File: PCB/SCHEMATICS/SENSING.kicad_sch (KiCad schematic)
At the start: 7 parts, among them U3 LTR-303ALS-01

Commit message: Updated Schematics
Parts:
- removed R6: 1K, symbol Device:R_Small_US
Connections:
- net VBUS is gone; now on net +3.3V: R4.1, R5.1
- net 1 renamed Battery_sensor_output
- net PB10 renamed Light_sensor_SCL
- net PB11 renamed Light_sensor_SDA
- net PINSSSS renamed GND
- net V3OUT renamed +3.3V
- net Vout renamed Vbatt
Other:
- moved on the sheet: R7, R8

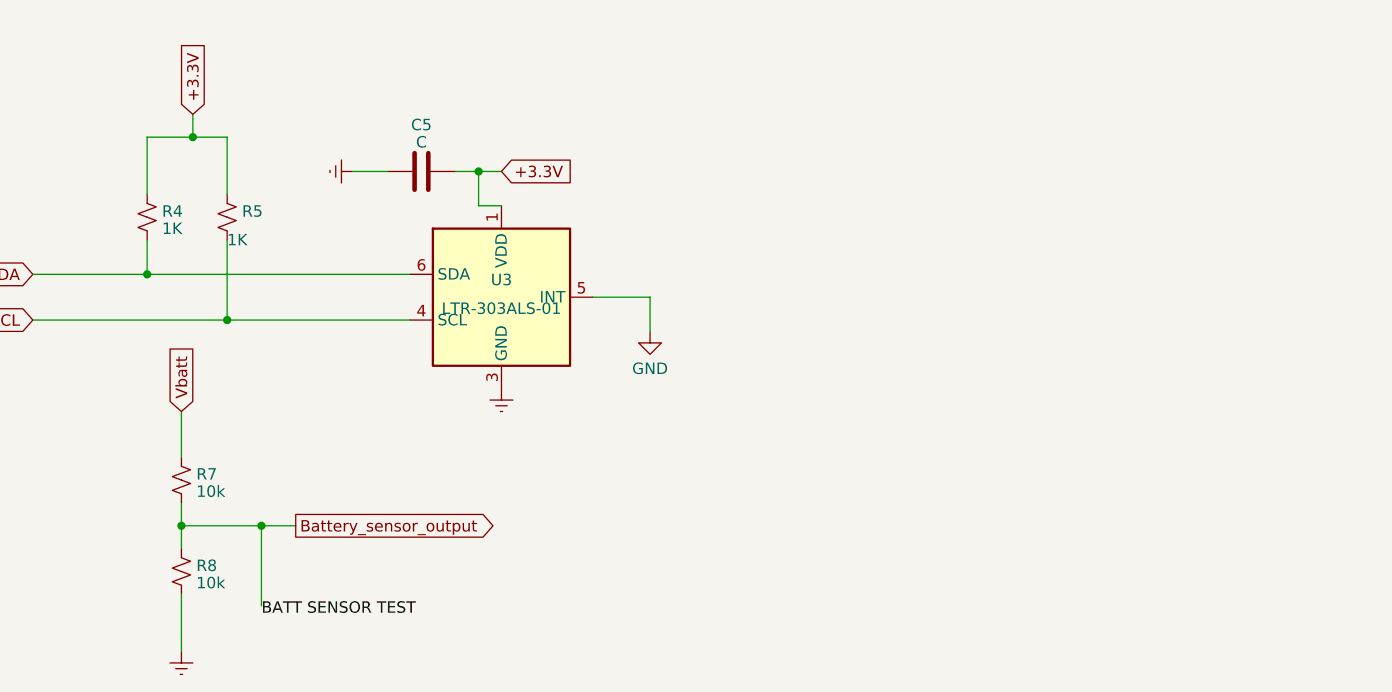
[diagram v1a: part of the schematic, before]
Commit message: UPDATED SCHEMATICS.
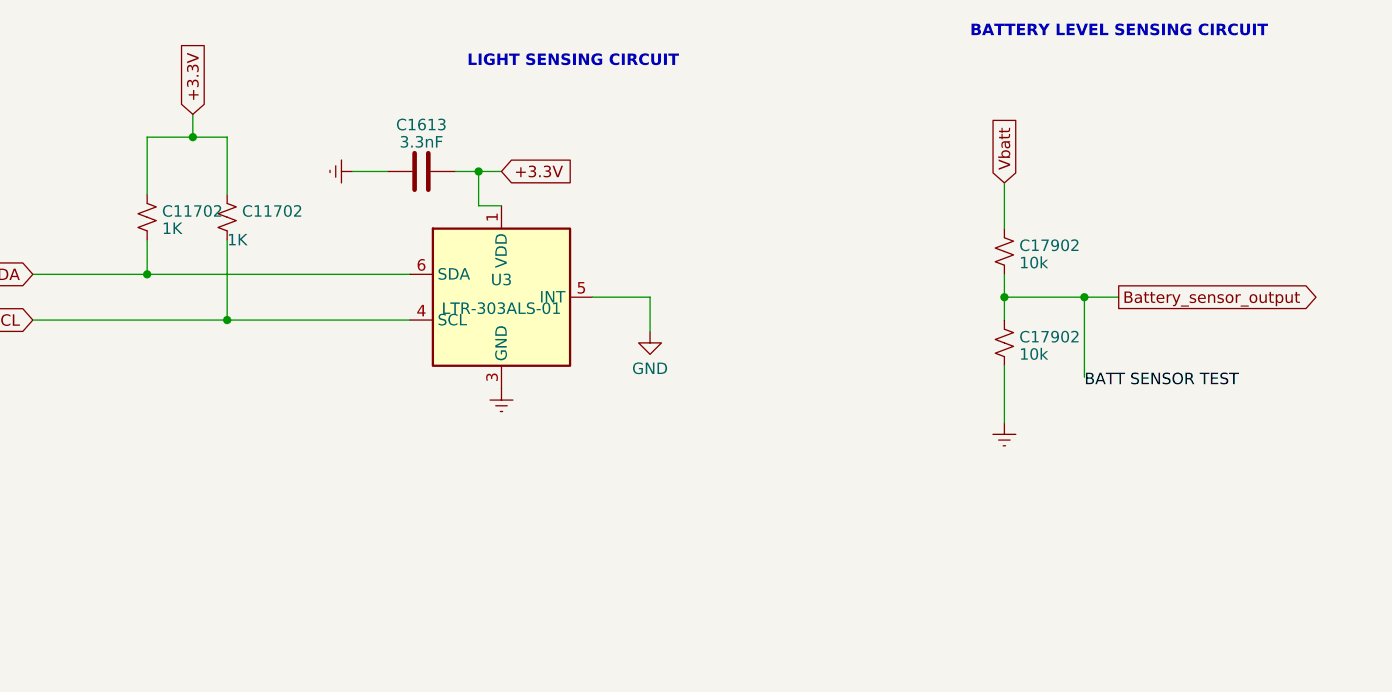
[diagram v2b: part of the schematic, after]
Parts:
- C11702: renamed from R4; Unit Price (none) -> 0.0005
- C11702: renamed from R5; Unit Price (none) -> 0.0005
- C1613: renamed from C5; value C -> 3.3nF; Unit Price (none) -> 0.0058
- C17902: renamed from R7; Unit Price (none) -> 0.003
- C17902: renamed from R8; Unit Price (none) -> 0.003
- U3: Extended (none) -> YES; Unit Price (none) -> 0.3887
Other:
- note added: "BATTERY LEVEL SENSING CIRCUIT"
- note added: "LIGHT SENSING CIRCUIT"
- moved on the sheet: C17902

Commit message: Updating schematics
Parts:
- added C1, C2: 1K, symbol Device:R_Small_US
- added C3: 3.3nF, symbol Device:C
- added TP1, TP2: TestPoint, symbol Connector:TestPoint
- added U5: LTR-303ALS-01, OptoDevice:Lite-On_LTR-303ALS-01, symbol Sensor_Optical:LTR-303ALS-01
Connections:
- net +3.3V: now also C1.1, C2.1, C3.2, U5.1 (VDD)
- net Earth: now also C3.1, U5.3 (GND)
- net GND: now also U5.5 (INT)
- new net: C1.2, TP1.1, U5.6 (SDA)
- new net: C2.2, TP2.1, U5.4 (SCL)

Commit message: Adjusted Schematics
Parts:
- added TP13, TP14, TP15, TP16, TP17, TP18, TP19, TP20, TP21: TestPoint, symbol Connector:TestPoint
- C17900: renamed from C17902; value 10k -> 100k
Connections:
- net Battery_sensor_output: now also TP21.1
- net Light_sensor_SCL: now also TP14.1, TP17.1
- net Light_sensor_SDA: now also TP15.1, TP16.1
- net +3.3V renamed 3V3
- net 3V3: now also TP13.1; no longer C1.1, C2.1, C3.2, U5.1 (VDD)
- net Vbatt renamed Battery
- net Battery: now also TP20.1
- new net: C3.2, TP18.1, U5.1 (VDD)
- new net: C1.1, C2.1, TP19.1
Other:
- note added: "Spare Light Sensor"
- moved on the sheet: C11702

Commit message: Updated schematics
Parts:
- C28323: renamed from C3; value 3.3nF -> 1uF
- C28323: renamed from C1613; value 3.3nF -> 1uF
- renumbered C1 to C11702, C2 to C11702
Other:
- company: (none) -> UCT
- title: (none) -> SENSING MODULE
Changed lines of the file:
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@@
 (kicad_sch (version 20230121) (generator eeschema)
   (paper "A4")
+  (title_block
+    (title "SENSING MODULE")
+    (company "UCT")
+    (comment 1 "Author: Ankush Chohan ")
+    (comment 2 "Version: 2")
+  )
   (junction (at 208.28 80.01) (diameter 0) (color 0 0 0 0)
   )
@@
   (symbol (lib_id "Device:C") (at 137.16 124.46 90) (unit 1)
     (in_bom yes) (on_board yes) (dnp no) (fields_autoplaced)
-    (property "Reference" "C3" (at 137.16 119.2911 90)
-      (effects (font (size 1.27 1.27)))
-    )
-    (property "Value" "3.3nF" (at 137.16 121.2121 90)
+    (property "Reference" "C28323" (at 137.16 118.11 90)
+      (effects (font (size 1.27 1.27)))
+    )
+    (property "Value" "1uF" (at 137.16 120.65 90)
       (effects (font (size 1.27 1.27)))
     )
@@
       (project "SCHEMATICS"
         (path "/c9ca3a5c-30cb-4dce-b611-3270b9f3284b/1428f64b-a76f-4ab8-8617-b5b39829c481"
-          (reference "C3") (unit 1)
+          (reference "C28323") (unit 1)
         )
       )
@@
   (symbol (lib_id "Device:R_Small_US") (at 106.68 129.54 0) (unit 1)
     (in_bom yes) (on_board yes) (dnp no) (fields_autoplaced)
-    (property "Reference" "C1" (at 108.331 128.8963 0)
-      (effects (font (size 1.27 1.27)) (justify left))
-    )
-    (property "Value" "1K" (at 108.331 130.8173 0)
+    (property "Reference" "C11702" (at 109.22 128.905 0)
+      (effects (font (size 1.27 1.27)) (justify left))
+    )
+    (property "Value" "1K" (at 109.22 131.445 0)
       (effects (font (size 1.27 1.27)) (justify left))
     )
@@
       (project "SCHEMATICS"
         (path "/c9ca3a5c-30cb-4dce-b611-3270b9f3284b/1428f64b-a76f-4ab8-8617-b5b39829c481"
-          (reference "C1") (unit 1)
+          (reference "C11702") (unit 1)
         )
       )
@@
   (symbol (lib_id "Device:R_Small_US") (at 115.57 129.54 0) (unit 1)
     (in_bom yes) (on_board yes) (dnp no)
-    (property "Reference" "C2" (at 117.221 128.8963 0)
+    (property "Reference" "C11702" (at 117.221 128.8963 0)
       (effects (font (size 1.27 1.27)) (justify left))
     )
@@
       (project "SCHEMATICS"
         (path "/c9ca3a5c-30cb-4dce-b611-3270b9f3284b/1428f64b-a76f-4ab8-8617-b5b39829c481"
-          (reference "C2") (unit 1)
+          (reference "C11702") (unit 1)
         )
       )
@@
   (symbol (lib_id "Device:C") (at 143.51 76.2 90) (unit 1)
     (in_bom yes) (on_board yes) (dnp no) (fields_autoplaced)
-    (property "Reference" "C1613" (at 143.51 71.0311 90)
-      (effects (font (size 1.27 1.27)))
-    )
-    (property "Value" "3.3nF" (at 143.51 72.9521 90)
+    (property "Reference" "C28323" (at 143.51 69.85 90)
+      (effects (font (size 1.27 1.27)))
+    )
+    (property "Value" "1uF" (at 143.51 72.39 90)
       (effects (font (size 1.27 1.27)))
     )
@@
       (project "SCHEMATICS"
         (path "/c9ca3a5c-30cb-4dce-b611-3270b9f3284b/1428f64b-a76f-4ab8-8617-b5b39829c481"
-          (reference "C1613") (unit 1)
-        )
-      )
+          (reference "C28323") (unit 1)
+        )
+      )

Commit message: Updated schematics
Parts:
- added C6 (x3): 0, symbol Device:R_Small_US
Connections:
- net Battery_sensor_output: now also C6.2; no longer C17900.1, C17900.2, TP21.1
- net Light_sensor_SCL: now also C6.1; no longer C11702.2, TP14.1, TP17.1, U3.4 (SCL)
- net Light_sensor_SDA: now also C6.1; no longer C11702.2, TP15.1, TP16.1, U3.6 (SDA)
- new net: C11702.2, C6.2, TP15.1, TP16.1, U3.6 (SDA)
- new net: C11702.2, C6.2, TP14.1, TP17.1, U3.4 (SCL)
- new net: C17900.1, C17900.2, C6.1, TP21.1
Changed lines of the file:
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@@
     (stroke (width 0) (type default))
   )
-  (wire (pts (xy 76.2 92.71) (xy 83.82 92.71))
-    (stroke (width 0) (type default))
-  )
-  (wire (pts (xy 76.2 87.63) (xy 80.01 87.63))
+  (wire (pts (xy 63.5 92.71) (xy 67.31 92.71))
+    (stroke (width 0) (type default))
+  )
+  (wire (pts (xy 63.5 87.63) (xy 67.31 87.63))
     (stroke (width 0) (type default))
   )
@@
     (stroke (width 0) (type default))
   )
+  (wire (pts (xy 72.39 87.63) (xy 80.01 87.63))
+    (stroke (width 0) (type default))
+  )
   (wire (pts (xy 111.76 120.65) (xy 115.57 120.65))
     (stroke (width 0) (type default))
@@
     (stroke (width 0) (type default))
   )
+  (wire (pts (xy 72.39 92.71) (xy 83.82 92.71))
+    (stroke (width 0) (type default))
+  )
   (wire (pts (xy 106.68 135.89) (xy 135.89 135.89))
     (stroke (width 0) (type default))
@@
     (stroke (width 0) (type default))
   )
+  (wire (pts (xy 227.965 90.17) (xy 229.87 90.17))
+    (stroke (width 0) (type default))
+  )
   (wire (pts (xy 208.28 80.01) (xy 208.28 82.55))
     (stroke (width 0) (type default))
@@
     (stroke (width 0) (type default))
   )
-  (wire (pts (xy 217.17 90.17) (xy 220.98 90.17))
+  (wire (pts (xy 217.17 90.17) (xy 222.885 90.17))
     (stroke (width 0) (type default))
   )
@@
     (effects (font (size 1.27 1.27) bold) (justify left bottom))
   )
-  (hierarchical_label "Light_sensor_SCL" (shape output) (at 76.2 92.71 180) (fields_autoplaced)
+  (hierarchical_label "Light_sensor_SCL" (shape output) (at 63.5 92.71 180) (fields_autoplaced)
     (effects (font (size 1.27 1.27)) (justify right))
   )
-  (hierarchical_label "Battery_sensor_output" (shape output) (at 220.98 90.17 0) (fields_autoplaced)
+  (hierarchical_label "Battery_sensor_output" (shape output) (at 229.87 90.17 0) (fields_autoplaced)
     (effects (font (size 1.27 1.27)) (justify left))
   )
@@
     (effects (font (size 1.27 1.27)) (justify left))
   )
-  (hierarchical_label "Light_sensor_SDA" (shape output) (at 76.2 87.63 180) (fields_autoplaced)
+  (hierarchical_label "Light_sensor_SDA" (shape output) (at 63.5 87.63 180) (fields_autoplaced)
     (effects (font (size 1.27 1.27)) (justify right))
   )
@@
     )
   )
+  (symbol (lib_id "Device:R_Small_US") (at 225.425 90.17 90) (unit 1)
+    (in_bom yes) (on_board yes) (dnp no) (fields_autoplaced)
+    (property "Reference" "C6" (at 225.425 85.09 90)
+      (effects (font (size 1.27 1.27)))
+    )
+    (property "Value" "0" (at 225.425 87.63 90)
+      (effects (font (size 1.27 1.27)))
+    )
+    (property "Footprint" "" (at 225.425 90.17 0)
+      (effects (font (size 1.27 1.27)) hide)
+    )
+    (property "Datasheet" "~" (at 225.425 90.17 0)
+      (effects (font (size 1.27 1.27)) hide)
+    )
+    (pin "1")
+    (pin "2")
+    (instances
+      (project "SCHEMATICS"
+        (path "/c9ca3a5c-30cb-4dce-b611-3270b9f3284b/c574ee02-103d-4bad-a8c0-5ec1707f609e"
+          (reference "C6") (unit 1)
+        )
+        (path "/c9ca3a5c-30cb-4dce-b611-3270b9f3284b/1428f64b-a76f-4ab8-8617-b5b39829c481"
+          (reference "C4177") (unit 1)
+        )
+      )
+    )
+  )
   (symbol (lib_id "Connector:TestPoint") (at 218.44 73.66 0) (unit 1)
     (in_bom yes) (on_board yes) (dnp no) (fields_autoplaced)
@@
     )
   )
+  (symbol (lib_id "Device:R_Small_US") (at 69.85 87.63 90) (unit 1)
+    (in_bom yes) (on_board yes) (dnp no) (fields_autoplaced)
+    (property "Reference" "C6" (at 69.85 82.55 90)
+      (effects (font (size 1.27 1.27)))
+    )
+    (property "Value" "0" (at 69.85 85.09 90)
+      (effects (font (size 1.27 1.27)))
+    )
+    (property "Footprint" "" (at 69.85 87.63 0)
+      (effects (font (size 1.27 1.27)) hide)
+    )
+    (property "Datasheet" "~" (at 69.85 87.63 0)
+      (effects (font (size 1.27 1.27)) hide)
+    )
+    (pin "1")
+    (pin "2")
+    (instances
+      (project "SCHEMATICS"
+        (path "/c9ca3a5c-30cb-4dce-b611-3270b9f3284b/c574ee02-103d-4bad-a8c0-5ec1707f609e"
+          (reference "C6") (unit 1)
+        )
+        (path "/c9ca3a5c-30cb-4dce-b611-3270b9f3284b/1428f64b-a76f-4ab8-8617-b5b39829c481"
+          (reference "C4177") (unit 1)
+        )
+      )
+    )
+  )
   (symbol (lib_id "Device:C") (at 143.51 76.2 90) (unit 1)
     (in_bom yes) (on_board yes) (dnp no) (fields_autoplaced)
@@
         )
       )
+    )
+  )
+  (symbol (lib_id "Device:R_Small_US") (at 69.85 92.71 90) (unit 1)
+    (in_bom yes) (on_board yes) (dnp no)
+    (property "Reference" "C6" (at 69.342 95.25 90)
+      (effects (font (size 1.27 1.27)))
+    )
+    (property "Value" "0" (at 69.85 90.805 90)
+      (effects (font (size 1.27 1.27)))
+    )
+    (property "Footprint" "" (at 69.85 92.71 0)
+      (effects (font (size 1.27 1.27)) hide)
+    )
+    (property "Datasheet" "~" (at 69.85 92.71 0)
+      (effects (font (size 1.27 1.27)) hide)
+    )
+    (pin "1")
+    (pin "2")
+    (instances
+      (project "SCHEMATICS"
+        (path "/c9ca3a5c-30cb-4dce-b611-3270b9f3284b/c574ee02-103d-4bad-a8c0-5ec1707f609e"
+          (reference "C6") (unit 1)
+        )
+        (path "/c9ca3a5c-30cb-4dce-b611-3270b9f3284b/1428f64b-a76f-4ab8-8617-b5b39829c481"
+          (reference "C4177") (unit 1)
+        )
+      )

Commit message: Updated BOM
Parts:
- C4, C5: renamed from C28323; PART  (none) -> C28323
- C6: PART  (none) -> C4177; Unit Price (none) -> 0.0012
- R18, R19, R20, R21: renamed from C11702; value 1K -> 1k; PART  (none) -> C11702
- R22, R23: renamed from C17900; PART  (none) -> C17900
- TP1: PART  (none) -> TP1
- TP13: PART  (none) -> TP13
- TP14: PART  (none) -> TP14
- TP15: PART  (none) -> TP15
- TP16: PART  (none) -> TP16
- TP17: PART  (none) -> TP17
- TP18: PART  (none) -> TP18
- TP19: PART  (none) -> TP19
- TP2: PART  (none) -> TP2
- TP20: PART  (none) -> TP20
- TP21: PART  (none) -> TP21
- U3, U5: PART  (none) -> C364577

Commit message: Updating schematics
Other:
- moved on the sheet: C4, C5, C6, R18, R19, R20, R21, R22, R23, TP1, TP13, TP14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
